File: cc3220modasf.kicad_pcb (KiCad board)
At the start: 4 copper layers, 48.5 x 69.6 mm, 110 parts, among them J1 Conn_02x10_Odd_Even, J10 Conn_01x02, J12 Conn_02x03_Odd_Even, J13 Conn_02x05_Counter_Clockwise, J14 Conn_01x02, J15 Conn_01x02, J16 Conn_01x02, J18 Conn_01x02, J19 Conn_01x02, J2 Conn_02x10_Odd_Even, J20 Conn_01x02, J21 Conn_01x03, J22 Conn_01x03, J26 Conn_01x03, J3 Conn_02x06_Odd_Even, J5 Conn_01x03, J6 Conn_01x03, J7 Conn_02x07_Odd_Even, J9 Conn_01x02, Q4 BSS138, Q5 TP0610T, Q6 BSS138, Q7 BSS138, SW2 SW_DIP_x01, U10 TMP006AIYZFR, U7 OPA4340UA, U9 CC3220MODASF12MONR

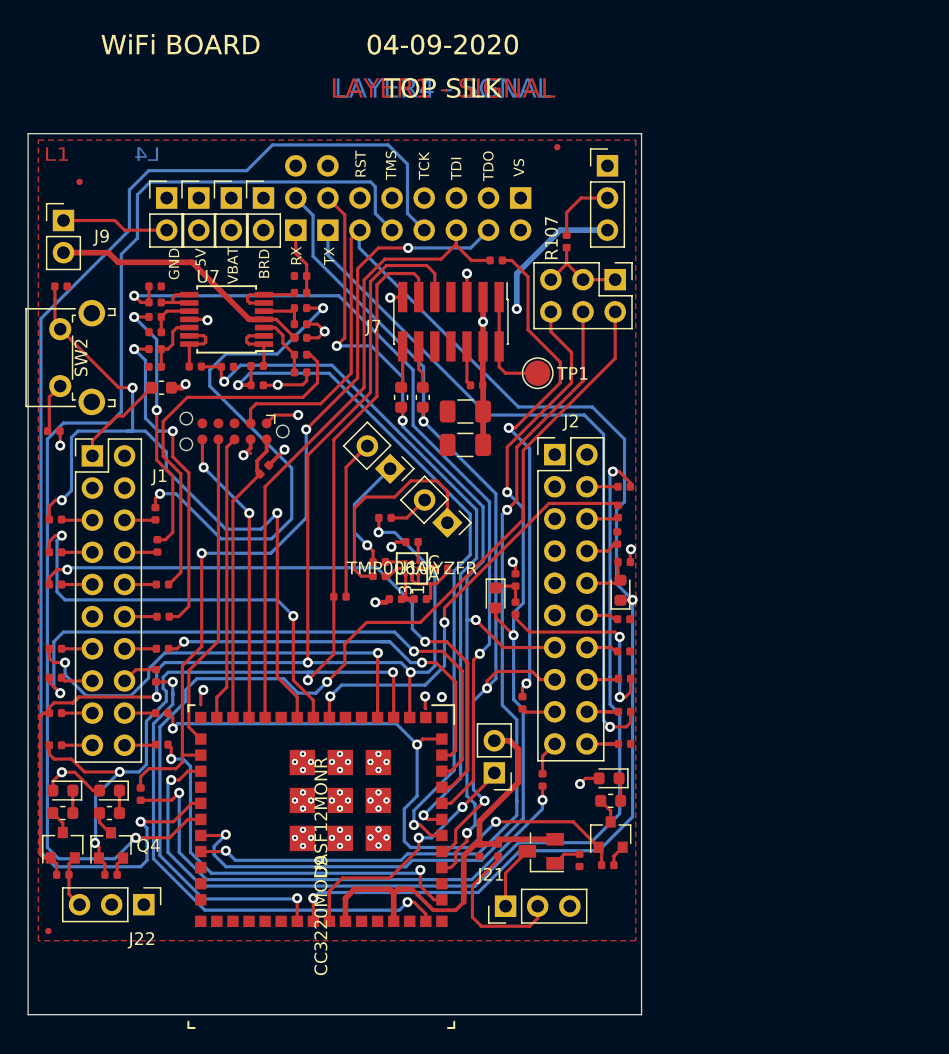
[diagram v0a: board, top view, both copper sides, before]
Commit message: Commit to record version prior to reducing board length to ~58mm
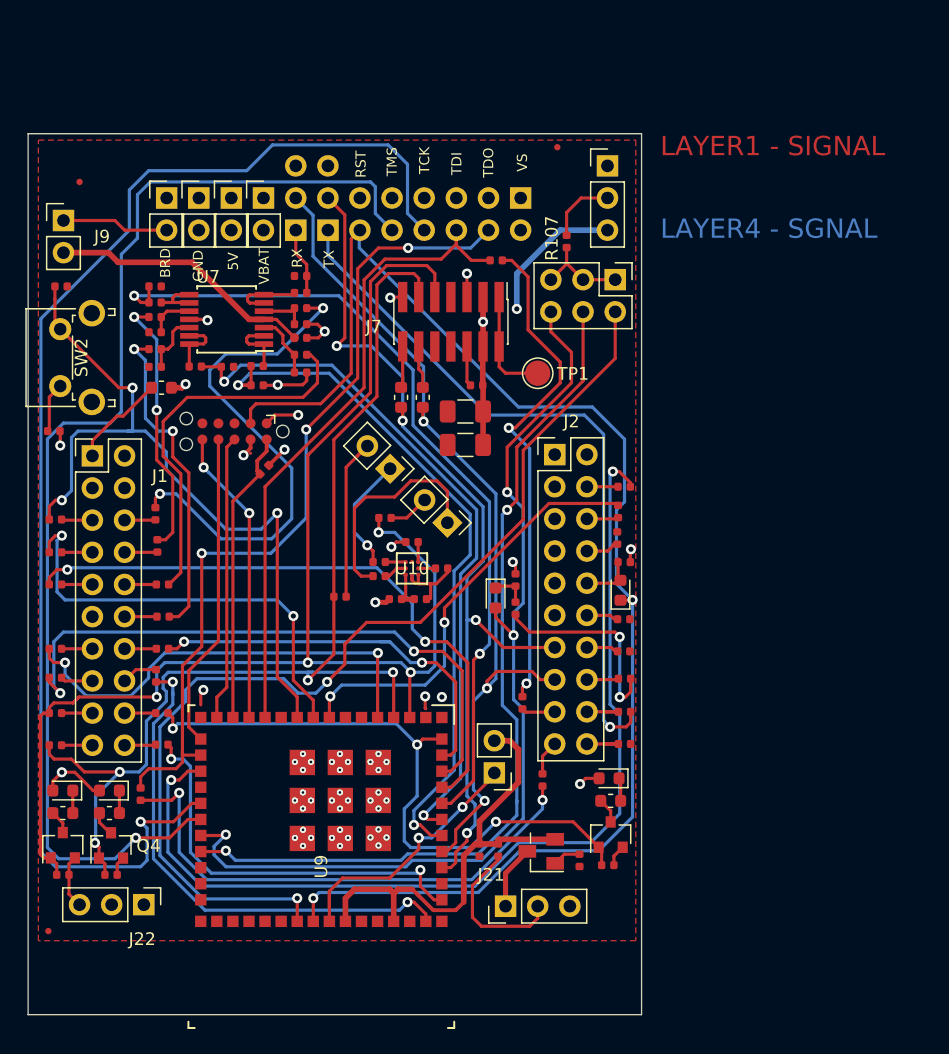
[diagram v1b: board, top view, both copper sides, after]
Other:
- board text added: "LAYER2 - GND (P.Cu)"
- board text added: "LAYER3 - POWER (G.Cu)"
- board text removed: "04-09-2020"
- board text removed: "BOTTOM PASTEMASK"
- board text removed: "BOTTOM SILK"
- board text removed: "BOTTOM SOLDERMASK"
- board text removed: "L1"
- board text removed: "L2"
- board text removed: "L4"
- board text removed: "LAYER2 - GND"
- board text removed: "LAYER3 - POWER"
- board text removed: "TOP PASTEMASK"
- board text removed: "TOP SILK"
- board text removed: "TOP SOLDERMASK"
- board text removed: "WiFi BOARD"

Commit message: Reduced board size to 49mmx57mm. Headers should now match pwrcon_1 commit from similar date
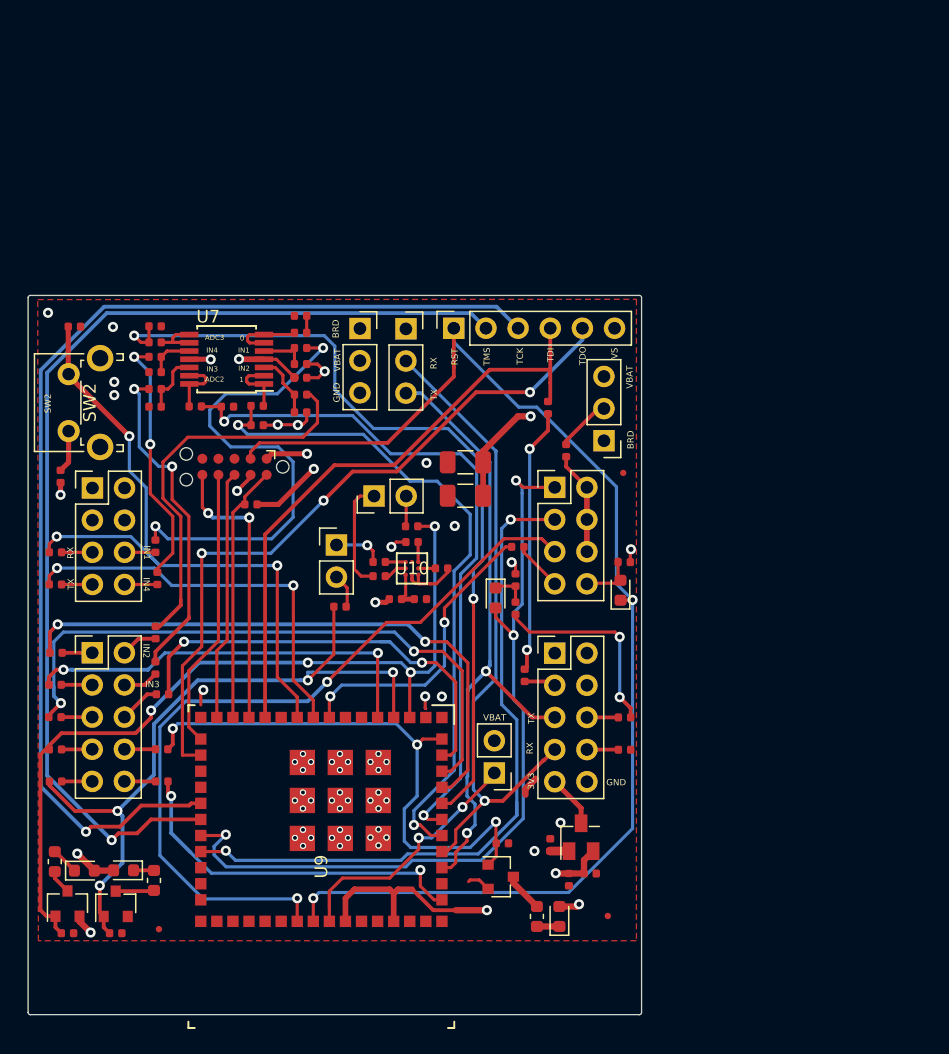
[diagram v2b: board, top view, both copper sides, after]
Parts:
- removed J12: Conn_02x03_Odd_Even, Connector_PinHeader_2.54mm:PinHeader_2x03_P2.54mm_Vertical
- removed J16, J18, J19, J20, J9: Conn_01x02, Connector_PinHeader_2.54mm:PinHeader_1x02_P2.54mm_Vertical
- removed J21: Conn_01x03, Connector_PinHeader_2.54mm:PinHeader_1x03_P2.54mm_Vertical
- removed J7: Conn_02x07_Odd_Even, Connector_PinHeader_1.27mm:PinHeader_2x07_P1.27mm_Vertical_SMD
- removed R104, R42, R46, R52, R56, R67, R68, R70: 0, Resistor_SMD:R_0402_1005Metric
- removed R31: 1K, Resistor_SMD:R_0402_1005Metric
- removed R33, R34: 33, Resistor_SMD:R_0603_1608Metric
- removed R38: 0, Resistor_SMD:R_0603_1608Metric
- removed TP1: TestPoint, TestPoint:TestPoint_Pad_D2.0mm
- added J11: Conn_02x04_Odd_Even, Connector_PinHeader_2.54mm:PinHeader_2x04_P2.54mm_Vertical, F.Cu at (81.3, 77.8)
- J1, J2: value Conn_02x10_Odd_Even -> Conn_02x05_Odd_Even; footprint Connector_PinHeader_2.54mm:PinHeader_2x10_P2.54mm_Vertical -> Connector_PinHeader_2.54mm:PinHeader_2x05_P2.54mm_Vertical
- J22: value Conn_01x03 -> Conn_02x04_Odd_Even; footprint Connector_PinHeader_2.54mm:PinHeader_1x03_P2.54mm_Vertical -> Connector_PinHeader_2.54mm:PinHeader_2x04_P2.54mm_Vertical
- J3: value Conn_02x06_Odd_Even -> Conn_01x06; footprint Connector_PinSocket_2.54mm:PinSocket_2x06_P2.54mm_Vertical -> Connector_PinSocket_2.54mm:PinSocket_1x06_P2.54mm_Vertical; moved to F.Cu
- J5, J6: moved to F.Cu
- moved FID3 71.4 mm to (122.0, 111.6)
- moved J22 46.3 mm to (117.8, 77.7), turned to 0 degrees
- moved FID1 26.3 mm to (123.2, 76.6)
- moved J26 21.7 mm to (121.7, 74.0), turned to 180 degrees
- moved R107 16.5 mm to (118.7, 74.8)
- moved J2 15.7 mm to (117.8, 90.8)
- moved J1 15.6 mm to (81.3, 90.8)
- moved R105 12.3 mm to (117.3, 71.4), turned to 270 degrees
- moved D10 11.6 mm to (118.2, 111.6), turned to 90 degrees
- moved J3 11.6 mm to (109.8, 65.2)
- moved R147 10.8 mm to (116.4, 111.6), turned to 90 degrees
- moved J5 9.94 mm to (106.0, 65.2)
- moved Q7 9.30 mm to (113.5, 108.5), turned to 0 degrees
- moved J6 9.28 mm to (102.4, 65.2)
- moved FID2 8.74 mm to (86.5, 112.6)
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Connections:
- C26 pad 2: /VCC_OPAMP -> /VCC_BRD
- J1 pad 1: /PWR -> /GPIO
- J1 pad 2: /VCC_5V -> Net-(J1-Pad2)
- J1 pad 3: (no net) -> Net-(J1-Pad3)
- J1 pad 4: GND -> Net-(J1-Pad4)
- J1 pad 5: /RX -> Net-(J1-Pad5)
- J1 pad 7: /TX -> Net-(J1-Pad7)
- J1 pad 9: /GPIO -> Net-(J1-Pad9)
- J2 pad 10: /LP_RESET_OUT -> GND
- J2 pad 2: GND -> (no net)
- J2 pad 3: (no net) -> Net-(J2-Pad3)
- J2 pad 4: Net-(J2-Pad4) -> (no net)
- J2 pad 5: (no net) -> /P55_GPIO_01
- J2 pad 7: (no net) -> /P57_GPIO_02
- J2 pad 9: (no net) -> Net-(J2-Pad9)
- J22 pad 1: /VCC_5V -> /SOP2
- J22 pad 2: GND -> Net-(J22-Pad2)
- J22 pad 3: GND -> /SOP1
- J3 pad 1: (no net) -> /CC_nRESET
- J3 pad 2: /VCC_BRD -> /P20_JTAG_TMS
- J3 pad 3: (no net) -> /P19_JTAG_TCK
- J3 pad 4: /P17_JTAG_TDO -> /P16_JTAG_TDI
- J3 pad 5: (no net) -> /P17_JTAG_TDO
- J3 pad 6: /P16_JTAG_TDI -> /VCC_BRD
- J5 pad 1: /LP_GPIO_01 -> (no net)
- J5 pad 2: /P55_GPIO_01 -> /P57_GPIO_02
- J5 pad 3: (no net) -> /P55_GPIO_01
- J6 pad 1: /LP_GPIO_02 -> /VCC_BRD
- J6 pad 2: /P57_GPIO_02 -> /VBAT_CC
- J6 pad 3: (no net) -> GND
- Q5 pad 3: Net-(J21-Pad1) -> Net-(J2-Pad9)
- R107 pad 1: Net-(J12-Pad1) -> Net-(J22-Pad2)
- R152 pad 1: Net-(Q5-Pad1) -> GND
- R152 pad 2: GND -> Net-(Q5-Pad1)
- R44 pad 1: /P08_GPIO_17 -> Net-(J22-Pad7)
- R44 pad 2: Net-(J2-Pad6) -> /P08_GPIO_17
- R50 pad 1: Net-(J1-Pad6) -> Net-(J11-Pad6)
- R54 pad 1: Net-(J1-Pad8) -> Net-(J11-Pad8)
- R58 pad 1: Net-(J1-Pad10) -> Net-(J1-Pad2)
- R60 pad 2: Net-(J2-Pad16) -> Net-(J2-Pad6)
- R62 pad 1: Net-(J1-Pad12) -> Net-(J1-Pad4)
- R63 pad 1: Net-(J2-Pad17) -> Net-(J2-Pad3)
- R64 pad 1: /LP_GPIO_01 -> (no net)
- R64 pad 2: Net-(J2-Pad18) -> Net-(J2-Pad8)
- R65 pad 1: Net-(J1-Pad13) -> Net-(J1-Pad3)
- R66 pad 1: Net-(J1-Pad14) -> Net-(J1-Pad6)
- R69 pad 1: Net-(J1-Pad15) -> Net-(J1-Pad5)
- R71 pad 1: Net-(J1-Pad17) -> Net-(J1-Pad7)
- R72 pad 1: Net-(J1-Pad18) -> Net-(J1-Pad8)
- R73 pad 1: Net-(J1-Pad19) -> Net-(J1-Pad9)
- R74 pad 1: Net-(J1-Pad20) -> Net-(J1-Pad10)
- U7 pad 4: /VCC_OPAMP -> /VCC_BRD
- U9 pad 19: /P18_GPIO_28 -> (no net)
- U9 pad 42: /P53_GPIO_30 -> (no net)
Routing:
- net /P18_GPIO_28: track 77.4 -> 0.00 mm, vias 2 -> 0
- net /VCC_5V: track 58.1 -> 0.00 mm
- net /LP_GPIO_01: track 55.6 -> 0.00 mm, vias 1 -> 0
- net /P17_GPIO_24: track 41.8 -> 0.00 mm, vias 2 -> 0
- net /P53_GPIO_30: track 40.6 -> 0.00 mm, vias 2 -> 0
- net /P01_GPIO_10: track 106.9 -> 66.4 mm
- net /P02_GPIO_11: track 87.9 -> 56.7 mm
- net /VCC_OPAMP: track 21.1 -> 0.00 mm
- net /P55_GPIO_01: track 71.3 -> 50.4 mm, vias 4 -> 2
- net /SOP0: track 81.6 -> 62.0 mm
- net /P16_GPIO_23: track 39.7 -> 20.9 mm
- net GND: track 45.8 -> 27.2 mm, vias 47 -> 53
- net /P57_GPIO_02: track 68.7 -> 51.7 mm, vias 3 -> 1
- net /VCC_BRD: track 20.4 -> 37.3 mm, vias 6 -> 8
- net /SOP1: track 69.8 -> 55.4 mm
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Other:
- board size 48.5 x 69.6 mm -> 48.5 x 56.8 mm
- board text added: "0"
- board text added: "1"
- board text added: "1.4mm +/- 20%"
- board text added: "3V3"
- board text added: "ADC2"
- board text added: "ADC3"
- board text added: "DIELECTRIC ------- FR4 - 0.255mm"
- board text added: "DIELECTRIC ------- FR4 - 0.700mm"
- board text added: "IN1"
- board text added: "IN2"
- board text added: "IN3"
- board text added: "IN4"
- board text added: "LAYER1 - SIGNAL - CU - 0.035mm"
- board text added: "LAYER2 - GROUND - CU - 0.035mm"
- board text added: "LAYER3 - POWER - CU - 0.035mm"
- board text added: "LAYER4 - SIGNAL - CU - 0.035mm"
- board text added: "SOLDERMASK / SILKSCREEEN 0.025mm"
- board text added: "SW2"
- board text removed: "5V"
- board text removed: "L3"
- board text removed: "LAYER1 - SIGNAL"
- board text removed: "LAYER2 - GND (P.Cu)"
- board text removed: "LAYER3 - POWER (G.Cu)"
- board text removed: "LAYER4 - SGNAL"
